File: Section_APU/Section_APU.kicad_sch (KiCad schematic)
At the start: 24 parts, among them J1 APU ribbon, J2 Backlight, SW1 APU MASTER SW, SW2 APU START

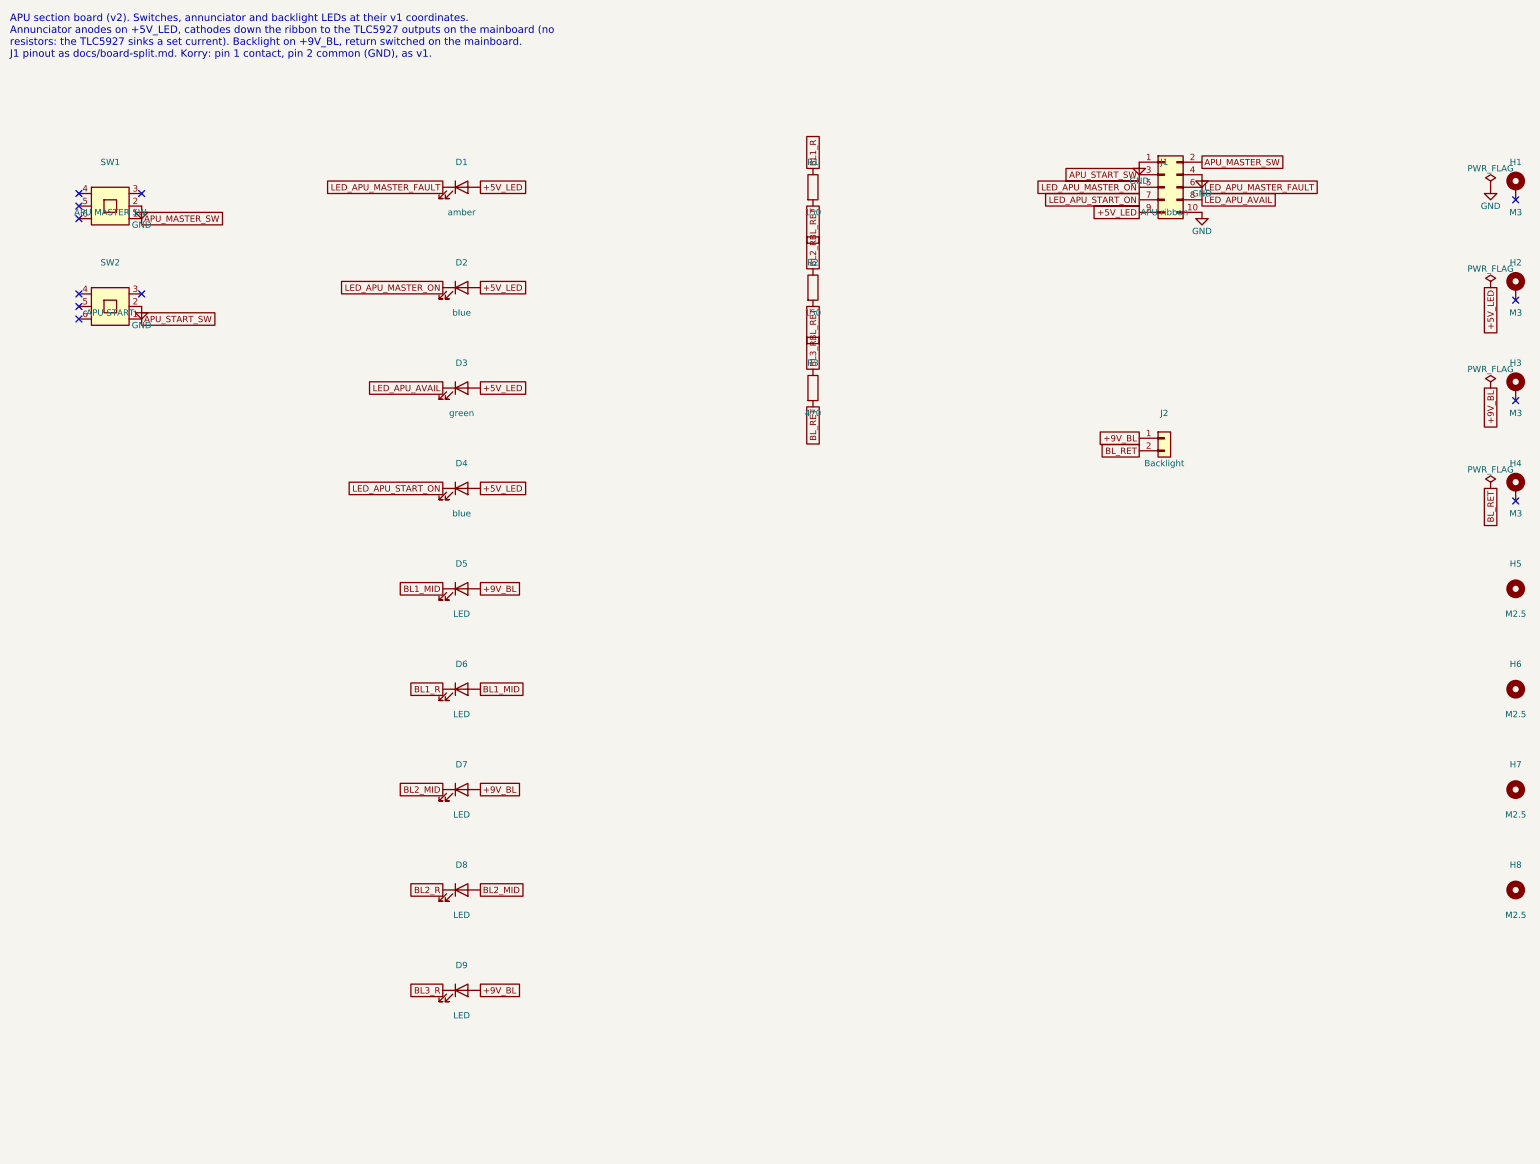
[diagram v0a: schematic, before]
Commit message: Tidy the APU schematic and put the board on its sheet
Schematic: parts in spaced groups on the 100 mil grid, reference and value
outside the symbol body, horizontal on rotated parts, and GND on sideways
pins as a label instead of a power symbol that crowded its neighbours.

PCB: moved by (-54, -80) mm onto the middle of the A4 sheet, grid origin at
v1's (0, 0), title block filled in. Rerouted: ERC 0, DRC 0, nothing
unconnected, no schematic-parity issues.

Co-Authored-By: Claude Opus 5.5 <noreply@anthropic.com>
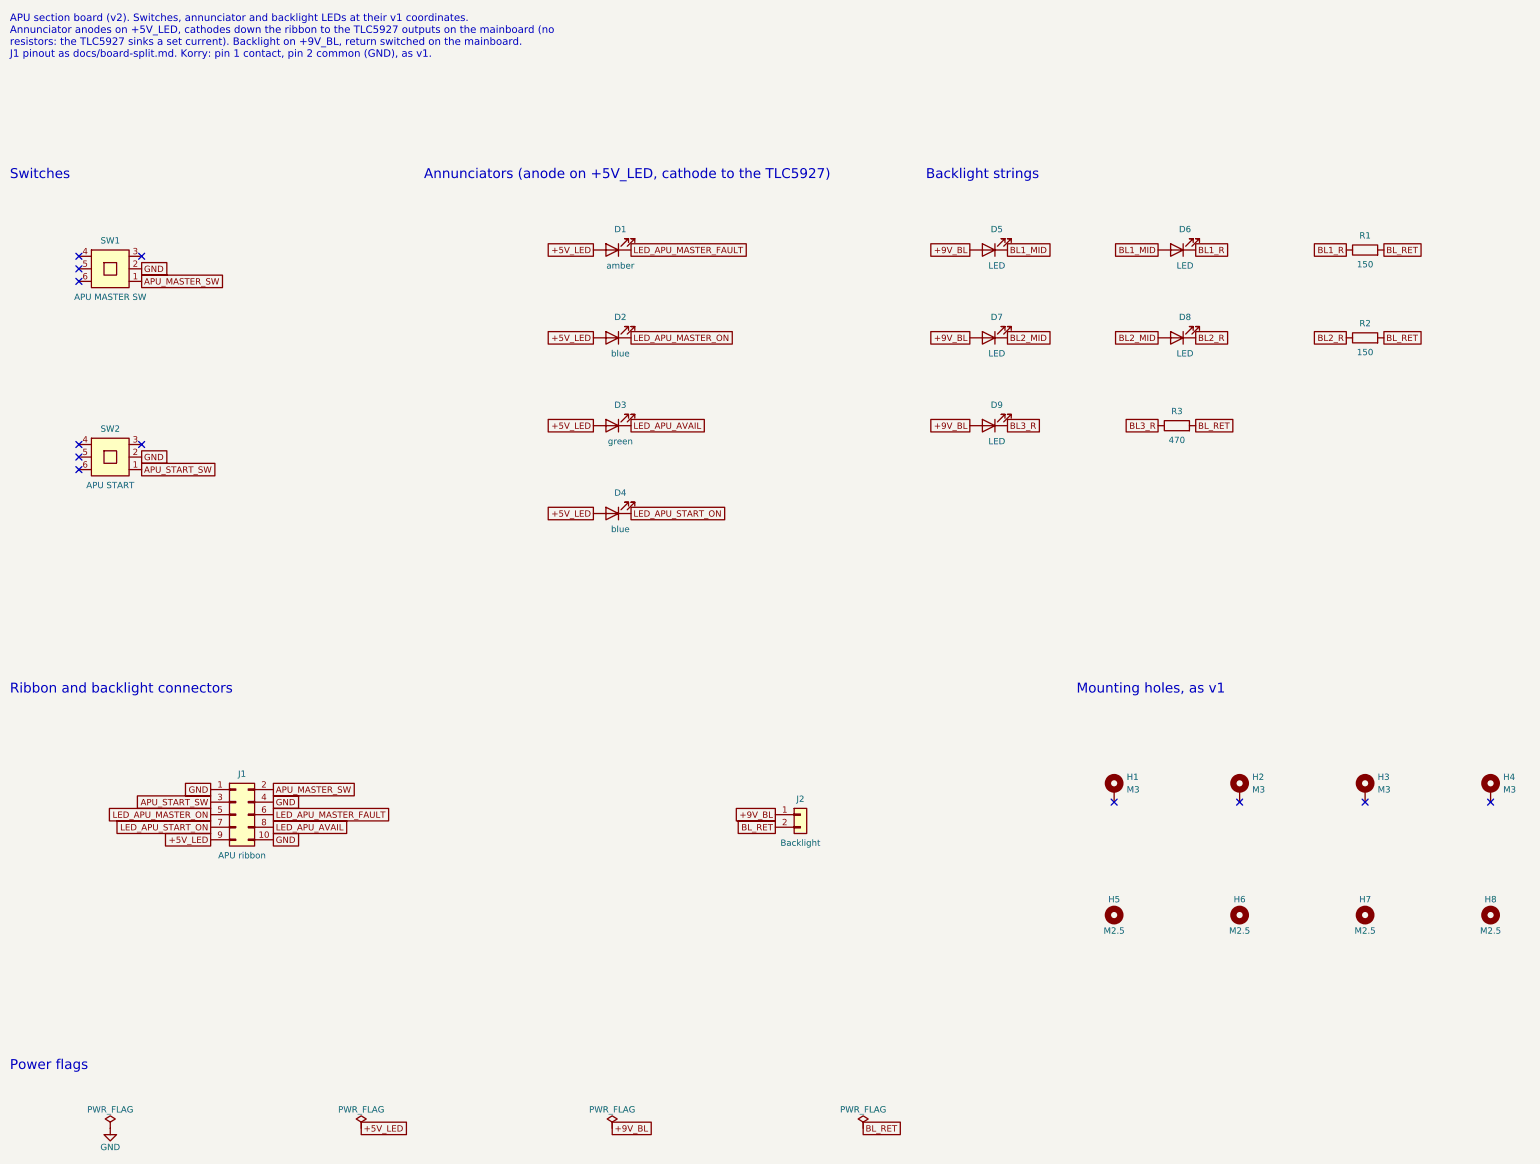
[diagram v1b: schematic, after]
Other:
- note added: "Annunciators (anode on +5V_LED, cathode to the TLC5927)"
- note added: "Backlight strings"
- note added: "Mounting holes, as v1"
- note added: "Power flags"
- note added: "Ribbon and backlight connectors"
- note added: "Switches"
